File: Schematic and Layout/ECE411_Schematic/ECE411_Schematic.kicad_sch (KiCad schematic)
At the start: 32 parts, among them J1 Raspberry Pi GPIO, J2 Raspberry_pi_audio_jack, M1 Motor_DC, U1 CAT24C256, U2 PCF8574, U3 LM386, U4 L293D Driver

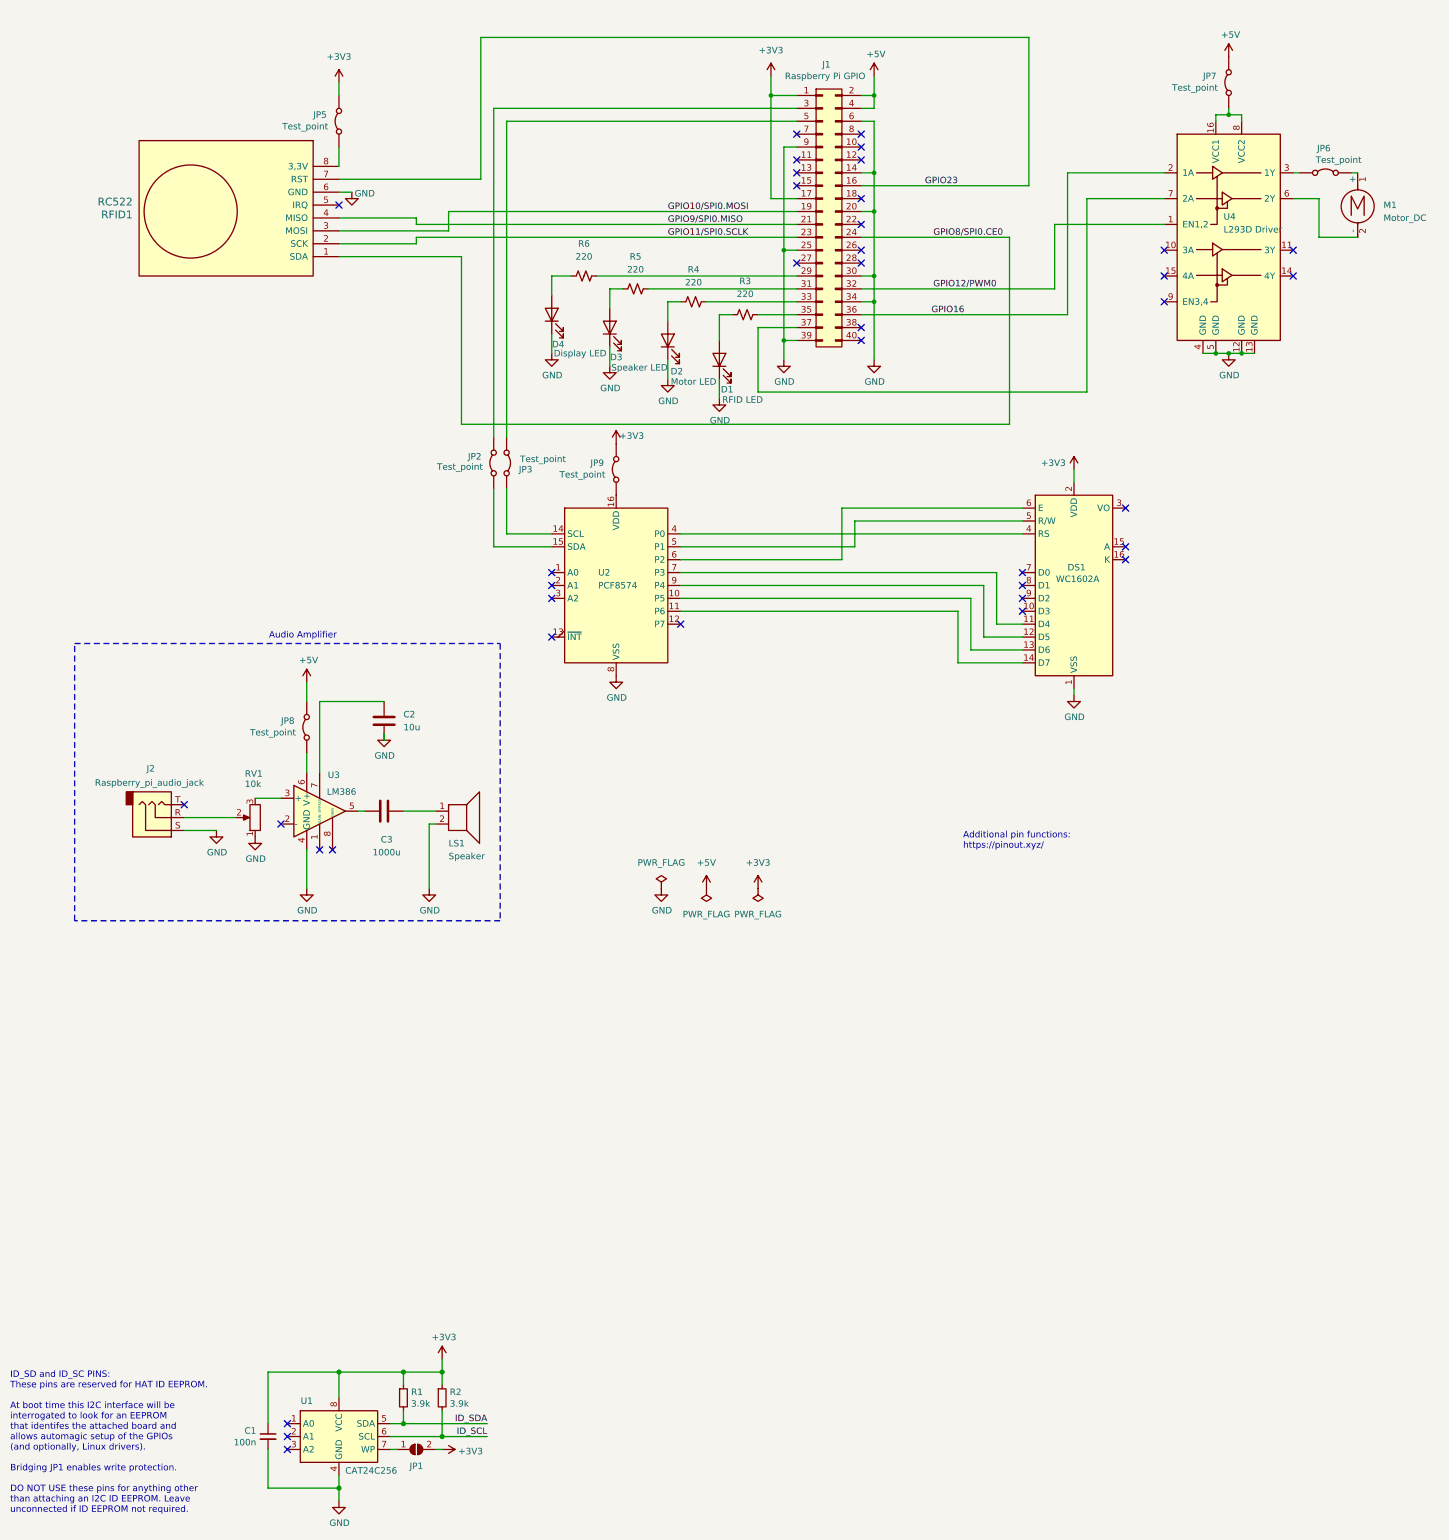
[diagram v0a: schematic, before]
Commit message: Version 6 schematic and Version 4 Layout
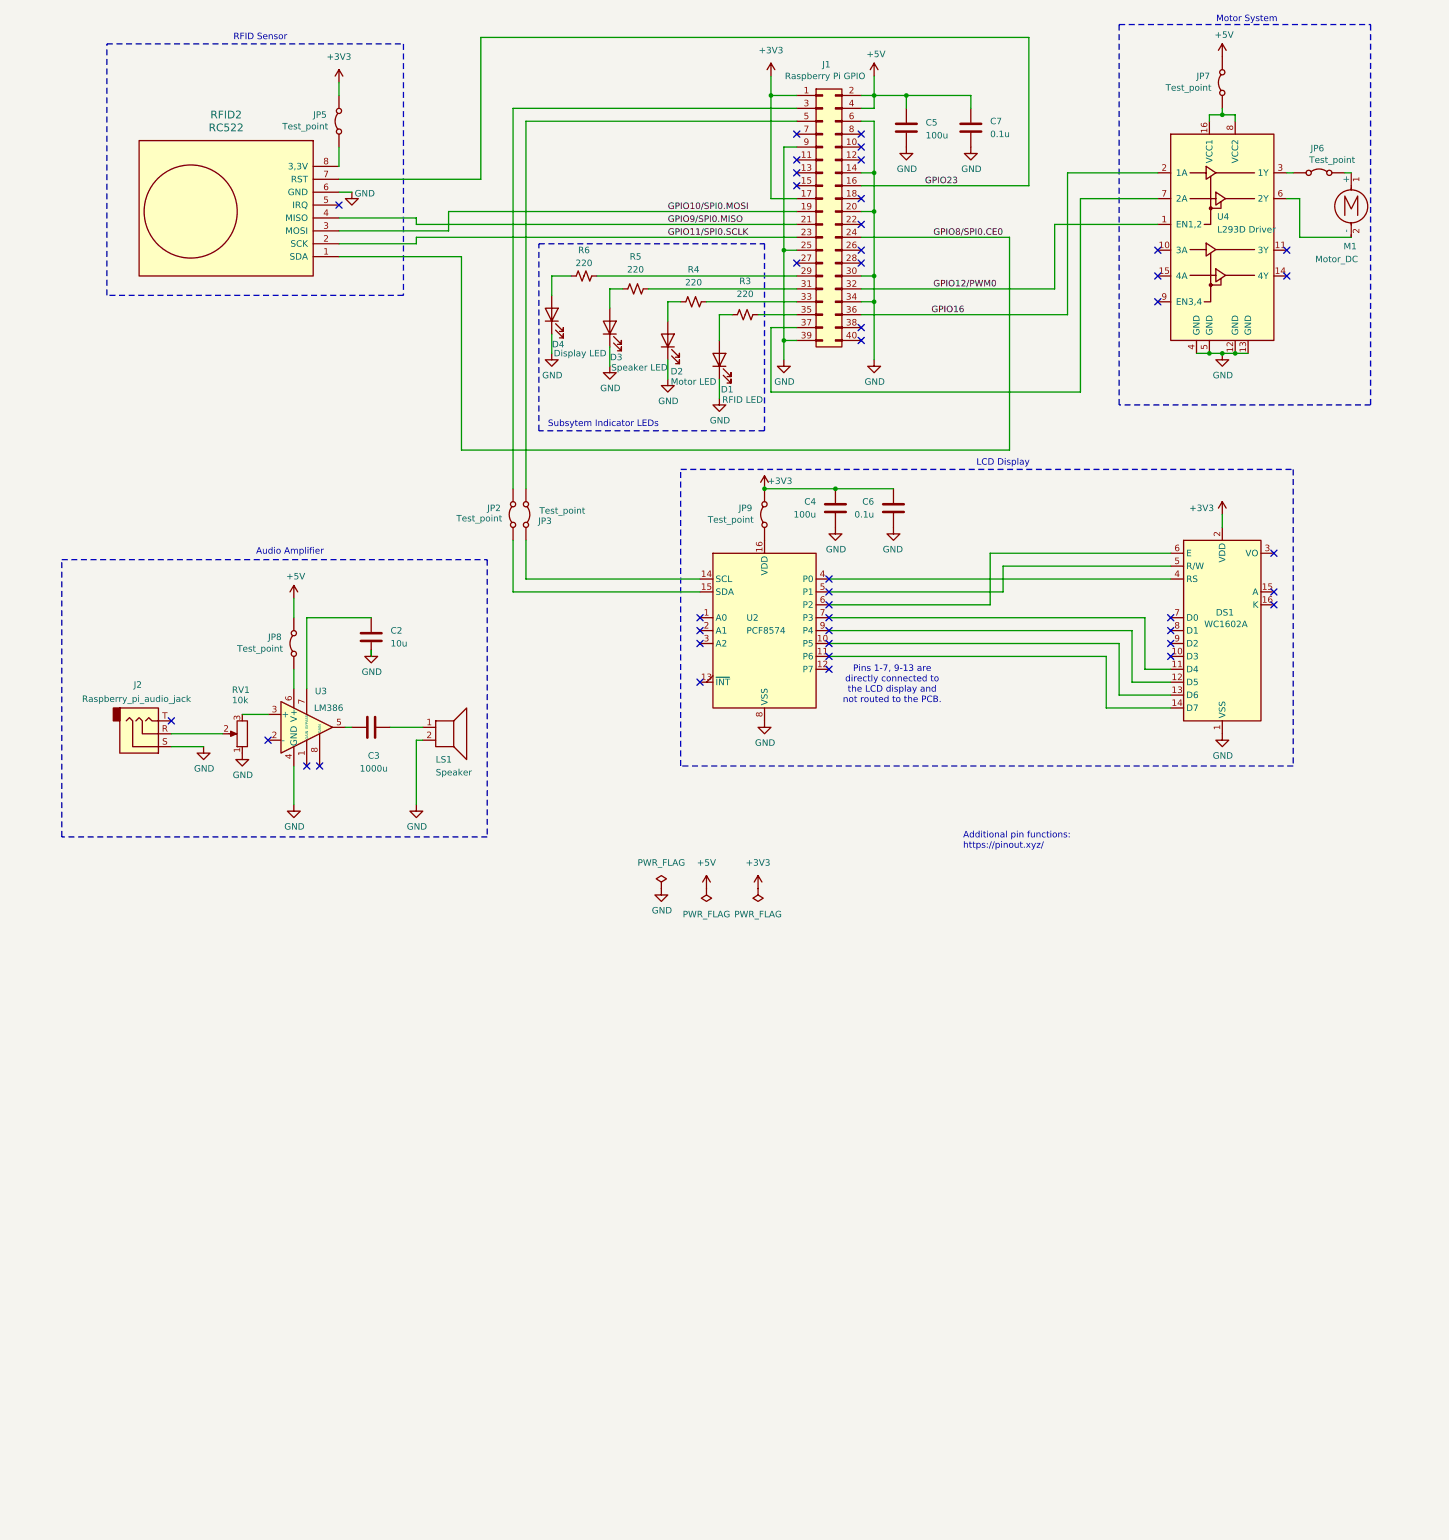
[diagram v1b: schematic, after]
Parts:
- removed C1: 100n, symbol Device:C_Small
- removed JP1: ID_WP, symbol Jumper:SolderJumper_2_Open
- removed R1, R2: 3.9k, symbol Device:R_Small
- removed RFID1: RC522, spotify_player_components:RC522, symbol spotify_player_components:RC522
- removed U1: CAT24C256, symbol Memory_EEPROM:CAT24C256
- added C4, C5: 100u, Capacitor_SMD:C_0805_2012Metric_Pad1.18x1.45mm_HandSolder, symbol Device:C
- added C6, C7: 0.1u, Capacitor_SMD:C_0805_2012Metric_Pad1.18x1.45mm_HandSolder, symbol Device:C
- added RFID2: RC522, symbol spotify_player_components:RC522
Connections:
- net +3V3: now also C4.1, C6.1
- net +5V: now also C5.1, C7.1
- net GND: now also C4.2, C5.2, C6.2, C7.2, RFID2.6 (GND)
- net GPIO10/SPI0.MOSI: now also RFID2.3 (MOSI)
- net GPIO11/SPI0.SCLK: now also RFID2.2 (SCK)
- net GPIO23: now also RFID2.7 (RST)
- net GPIO8/SPI0.CE0: now also RFID2.1 (SDA)
- net GPIO9/SPI0.MISO: now also RFID2.4 (MISO)
- net at JP5.1 (A): now also RFID2.8 (3,3V)
- no-connect marks 39 -> 43
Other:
- note added: "LCD Display"
- note added: "Motor System"
- note added: "Pins 1-7, 9-13 are directly connected to the LCD display and not routed to the PCB."
- note added: "RFID Sensor"
- note added: "Subsytem Indicator LEDs"
- note removed: "ID_SD and ID_SC PINS: These pins are reserved for HAT ID EEPROM. At boot time this I2C interface will be interrogated to look for an EEPROM that identifes the attached board and allows automagic setup of the GPIOs (and optionally, Linux drivers). Bridging JP1 enables write protection. DO NOT USE these pins for anything other than attaching an I2C ID EEPROM. Leave unconnected if ID EEPROM not requ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"
- moved on the sheet: C2, C3, DS1, J2, JP2, JP3, JP6, JP7, JP8, JP9, LS1, M1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

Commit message: Final layout and schematic
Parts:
- DS1: value WC1602A -> LCD Display
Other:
- note added: "LCD System"
- note removed: "LCD Display"
- moved on the sheet: C5, C7, JP6, JP7, M1, U4
